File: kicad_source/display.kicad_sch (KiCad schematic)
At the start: 7 parts, among them J1 Conn_01x08

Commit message: added push button
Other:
- title: CyphalIMUBase/CAN -> CyphalHMIBase/CAN
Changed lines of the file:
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@@
 	(paper "A4")
 	(title_block
-		(title "CyphalIMUBase/CAN")
+		(title "CyphalHMIBase/CAN")
 		(date "2026-06-05")
 		(rev "0.1")

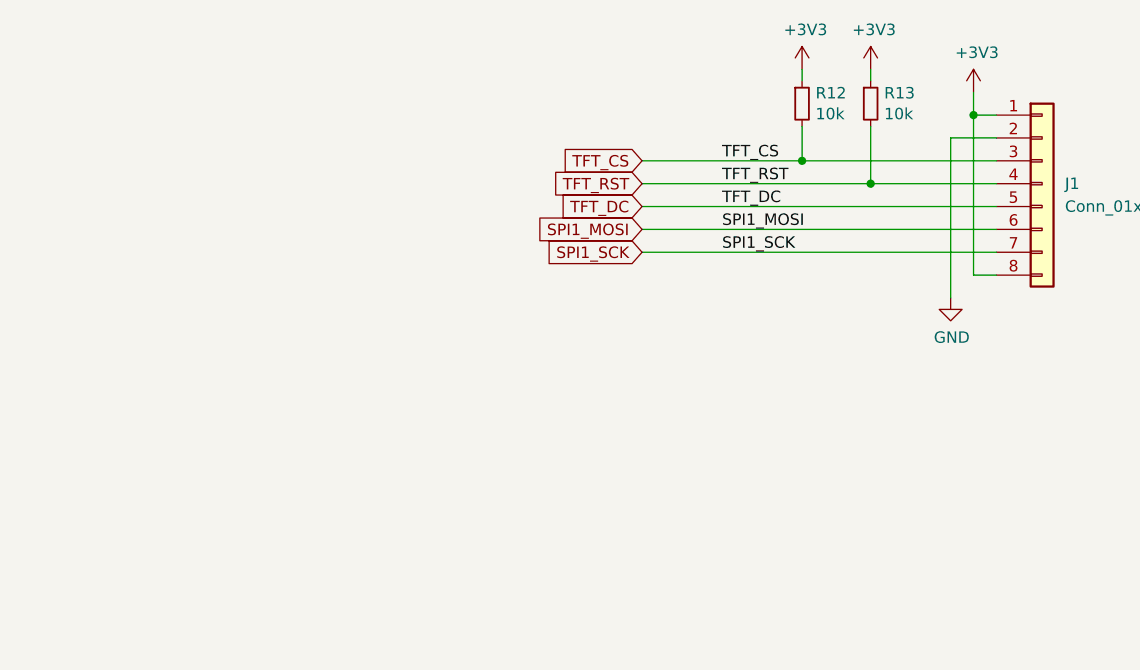
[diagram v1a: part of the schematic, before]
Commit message: added backlight control
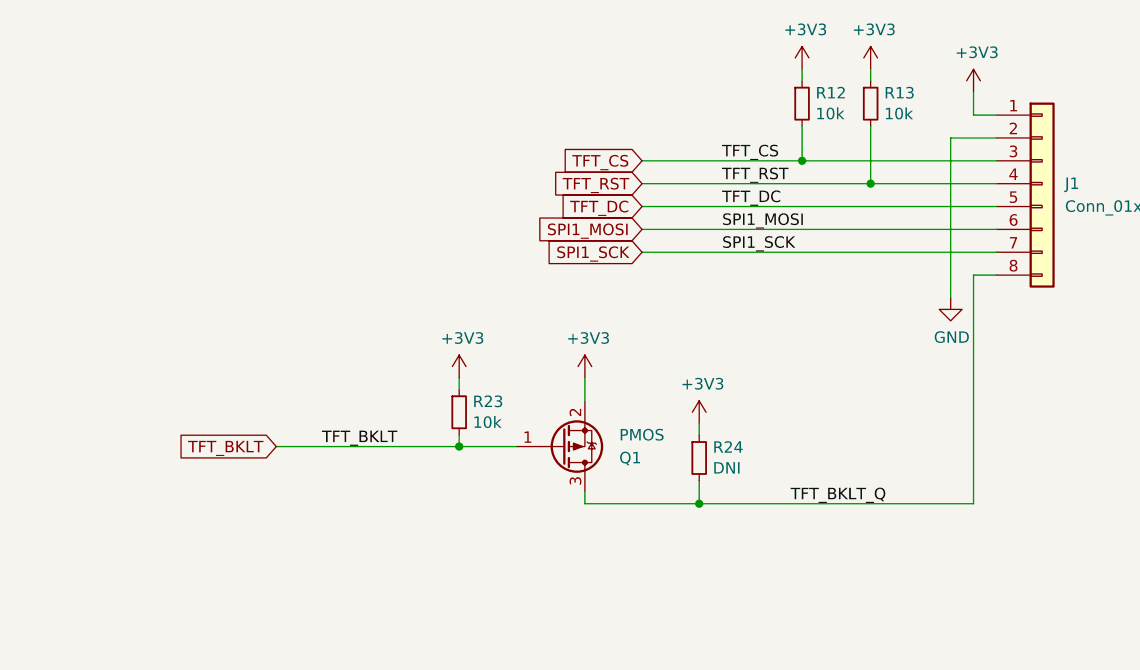
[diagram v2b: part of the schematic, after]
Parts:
- added Q1: PMOS, Package_TO_SOT_SMD:SOT-23, symbol Device:Q_PMOS_GSD
- added R23: 10k, Resistor_SMD:R_0603_1608Metric, symbol Device:R_Small
- added R24: DNI, Resistor_SMD:R_0603_1608Metric, symbol Device:R_Small
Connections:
- net +3V3: now also Q1.2 (S), R23.1, R24.1; no longer J1.8 (Pin_8)
- new net TFT_BKLT: Q1.1 (G), R23.2
- new net TFT_BKLT_Q: J1.8 (Pin_8), Q1.3 (D), R24.2
